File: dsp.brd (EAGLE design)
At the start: 190 x 113 mm, 131 parts, among them IC1 OPA2134P, IC2 OPA2134P, IC3 OPA2134P, U1 STM32F405RGT6, U2 CODECODER-WM8731SEDS/V(SSOP28), U4 LM2575HVS-3.3/NOPB, X1 ABLS-8.000MHZ-B4-T

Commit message: fixed grounds problem on codec (post fab)
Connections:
- removed net AGND: U2.15
- removed net DGND: U2.28
- net GND: now also U2.15, U2.28
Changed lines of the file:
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@@
 <via x="43.18" y="92.456" extent="1-16" drill="0.7"/>
 <contactref element="IC3" pad="5"/>
+<contactref element="U2" pad="15"/>
+<contactref element="U2" pad="28"/>
 </signal>
 <signal name="3.3V">
@@
 <wire x1="35.56" y1="54.356" x2="34.544" y2="53.34" width="0.4064" layer="16"/>
 </signal>
-<signal name="AGND">
-<contactref element="U2" pad="15"/>
-</signal>
-<signal name="DGND">
-<contactref element="U2" pad="28"/>
-</signal>
 <signal name="N$5">

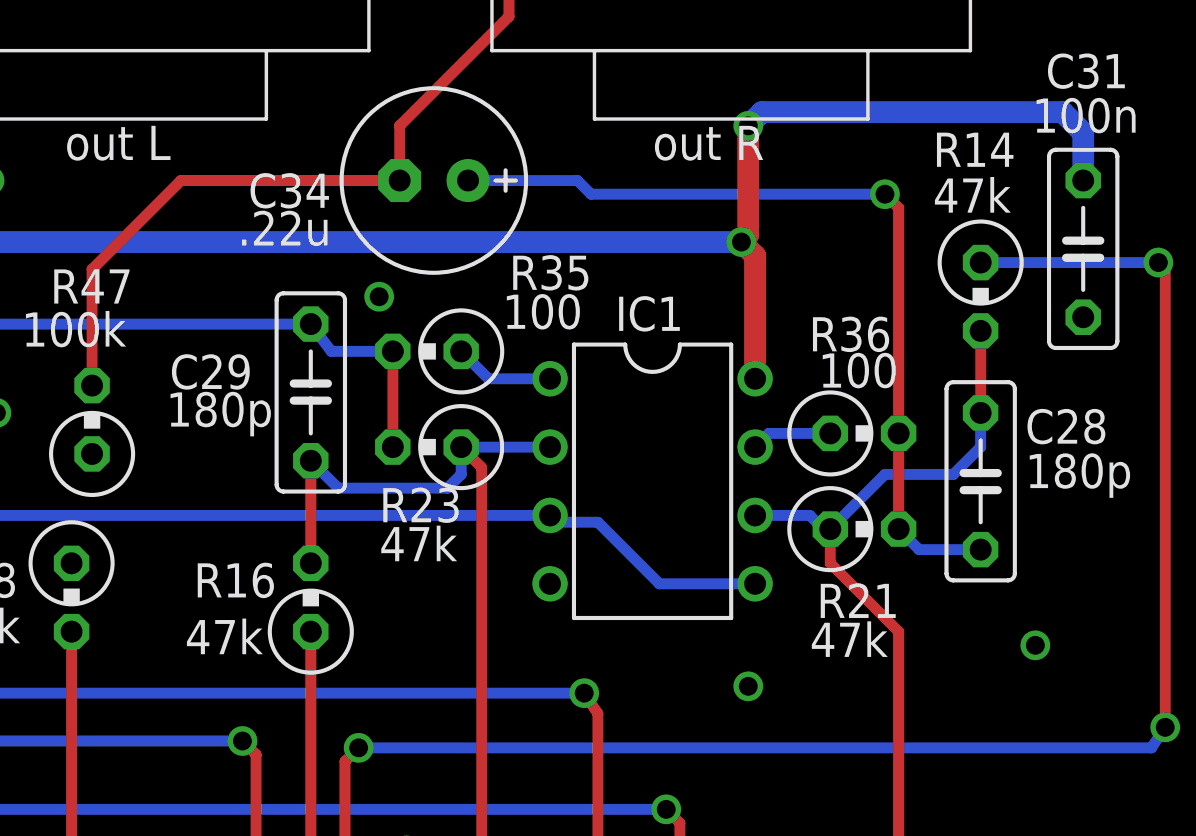
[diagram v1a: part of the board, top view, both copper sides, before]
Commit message: updated mixer resistors for higher wet amplitude
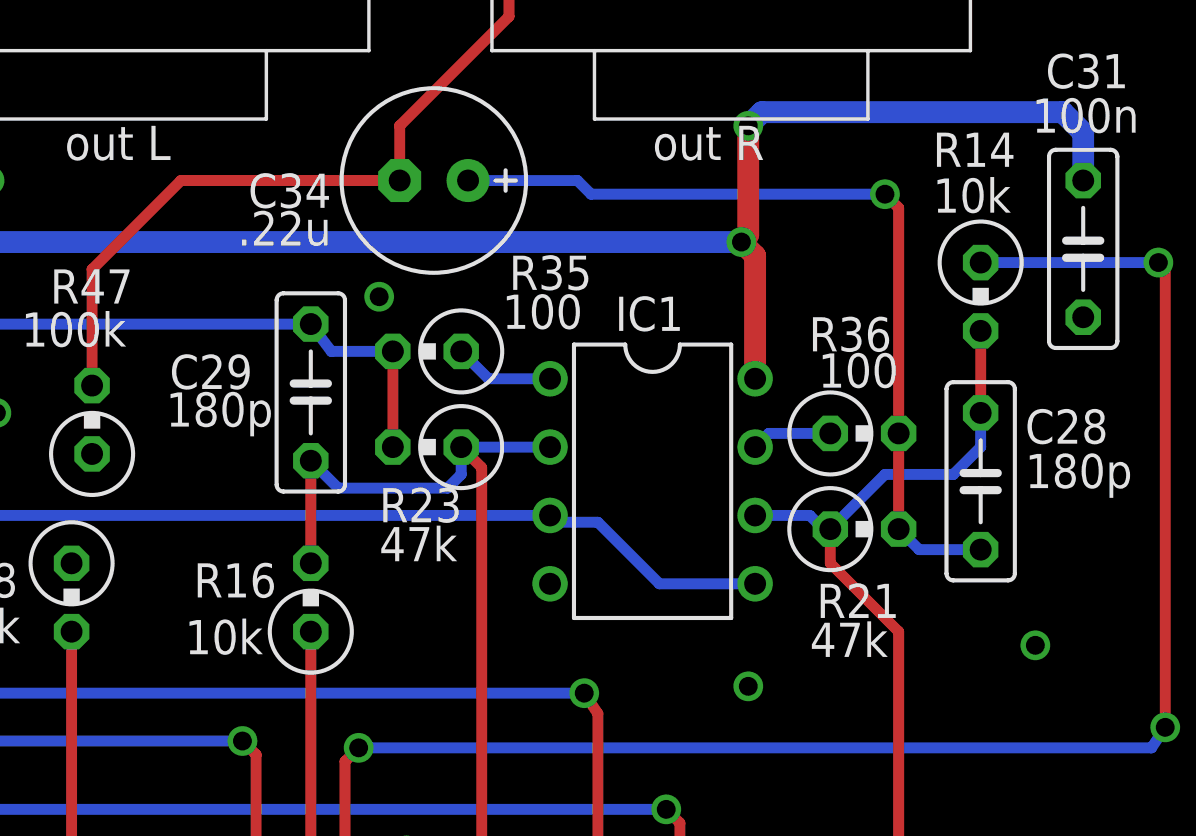
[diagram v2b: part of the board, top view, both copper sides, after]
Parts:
- R14, R16: value 47k -> 10k
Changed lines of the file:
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@@
 <attribute name="VALUE" x="84.836" y="81.3562" size="1.27" layer="21" font="vector" ratio="15"/>
 </element>
-<element name="R14" library="dan" package="0309V" value="47k" x="180.34" y="82.804" smashed="yes" rot="R270">
+<element name="R14" library="dan" package="0309V" value="10k" x="180.34" y="82.804" smashed="yes" rot="R270">
 <attribute name="NAME" x="178.562" y="87.63" size="1.27" layer="21" font="vector" ratio="15"/>
 <attribute name="VALUE" x="178.562" y="85.9282" size="1.27" layer="21" font="vector" ratio="15"/>
@@
 <attribute name="VALUE" x="100.076" y="24.3078" size="1.27" layer="21" font="vector" ratio="15" rot="R180"/>
 </element>
-<element name="R16" library="dan" package="0309V" value="47k" x="155.448" y="71.628" smashed="yes" rot="R90">
+<element name="R16" library="dan" package="0309V" value="10k" x="155.448" y="71.628" smashed="yes" rot="R90">
 <attribute name="NAME" x="154.178" y="72.898" size="1.27" layer="21" font="vector" ratio="15" rot="R180"/>
 <attribute name="VALUE" x="153.67" y="70.7898" size="1.27" layer="21" font="vector" ratio="15" rot="R180"/>
